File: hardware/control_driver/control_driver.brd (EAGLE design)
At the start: 90 x 37 mm, 73 parts, among them IC1 USB6B1, IC2 ADuM1250ARZ, IC3 ADuM1250ARZ, IC4 LM317LD, IC5 LM317LD, IC6 CP2102, IC7 AT24C512, IC8 STM32F051K8U6, J1 22-27-2041-04, J2 22-27-2031-03

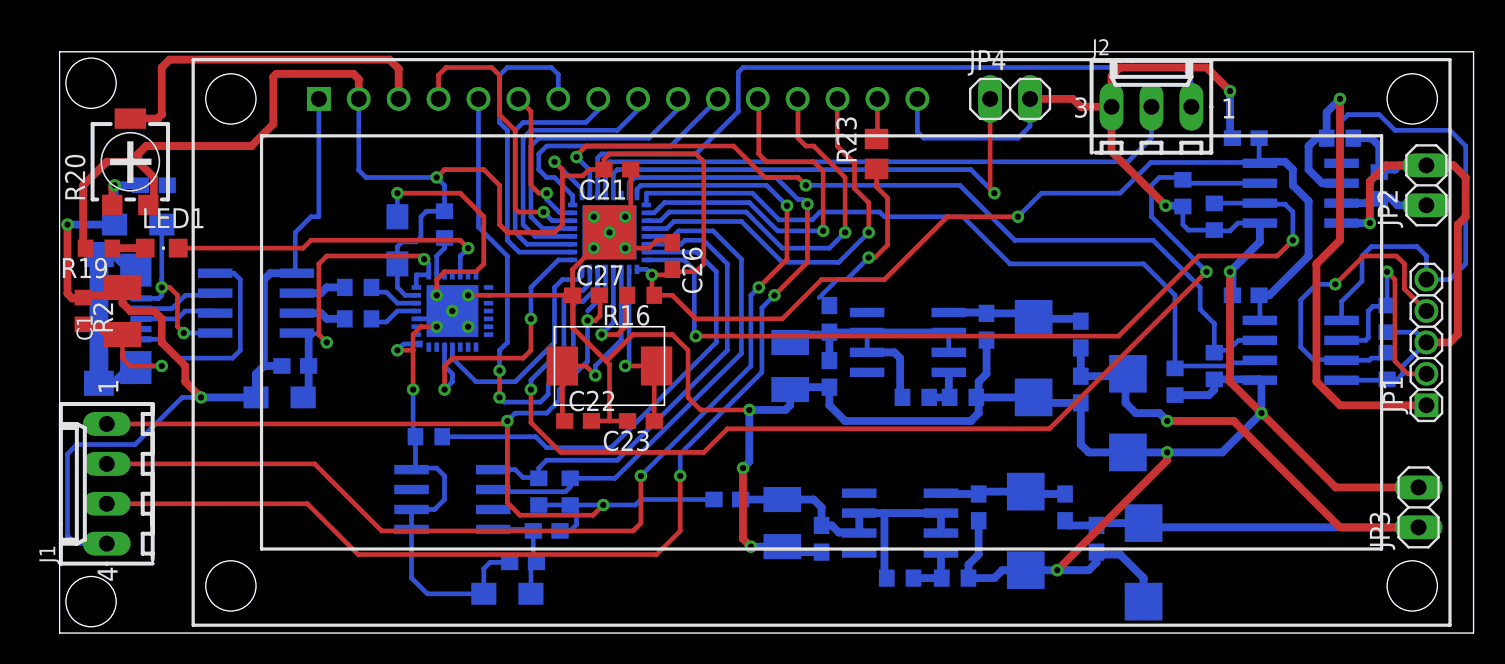
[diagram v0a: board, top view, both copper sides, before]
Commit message: Исправленые ошибки в трассировке платы управления
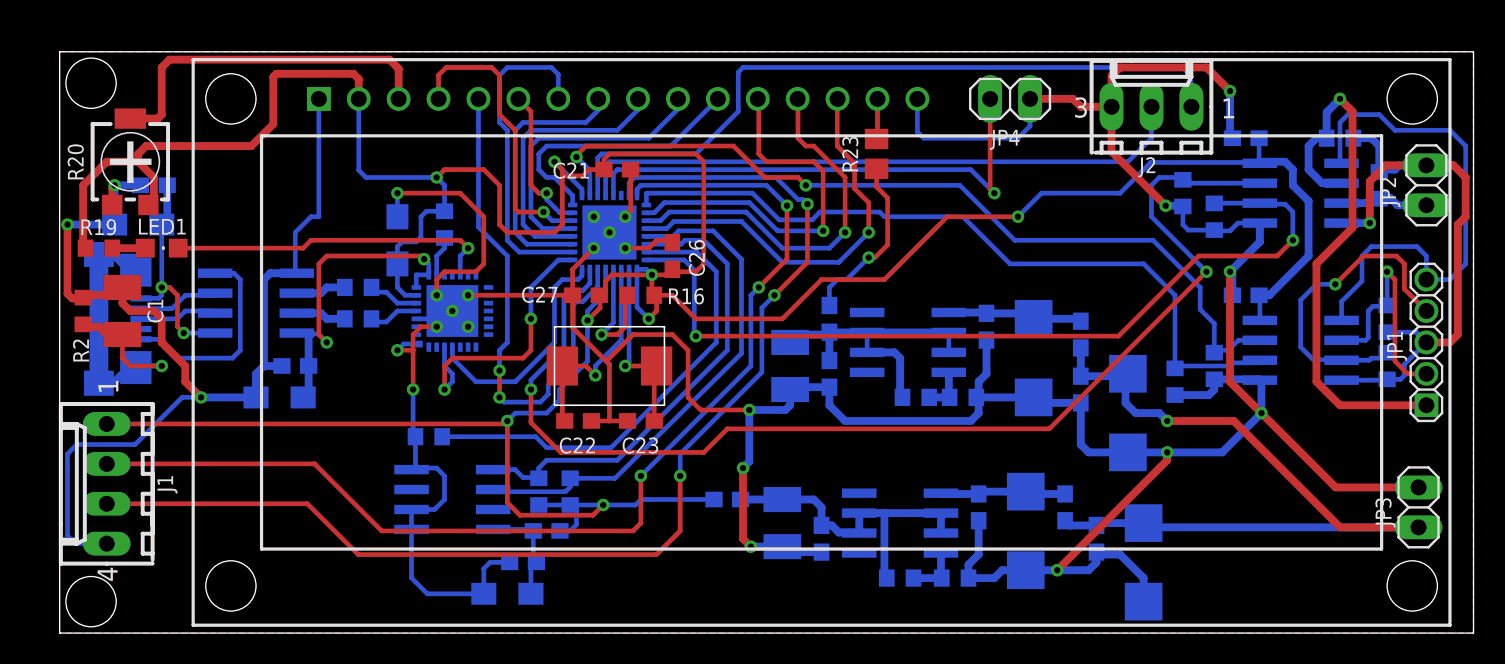
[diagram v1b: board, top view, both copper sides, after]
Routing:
- net VCC_3.3V: track 219.1 -> 229.0 mm, vias 7 -> 8
- net N$17: track 11.7 -> 14.3 mm
- net N$27: track 34.3 -> 34.9 mm
- net N$30: track 39.8 -> 40.0 mm, vias 2 -> 1
- added copper zone on layer 1, net GND
